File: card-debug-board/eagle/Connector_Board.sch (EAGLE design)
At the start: 32 parts, among them J1 ORESAT-DEBUG-CONNECTOR-CARD, J3 USB_A_SMT_FEMALE, Q1 MOSFET-PCH-SOT23-6, U1 FT230XS-R

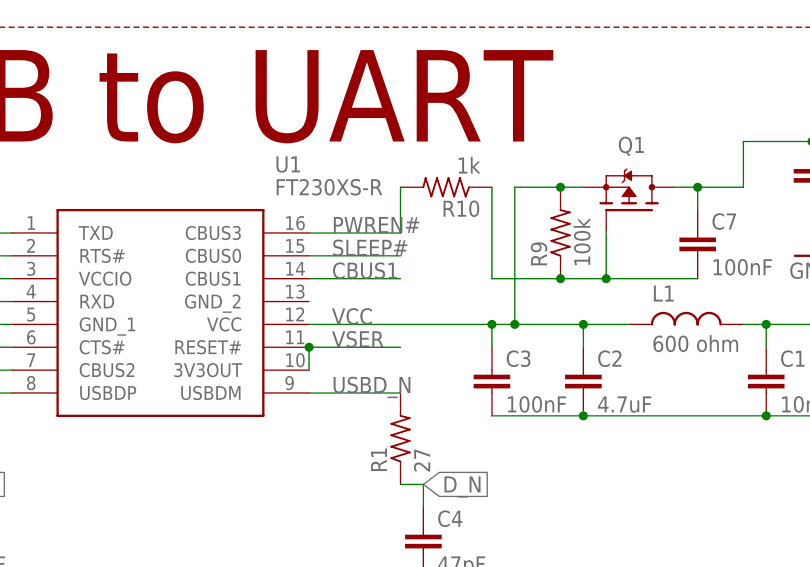
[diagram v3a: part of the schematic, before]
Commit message: clear all ERC errors
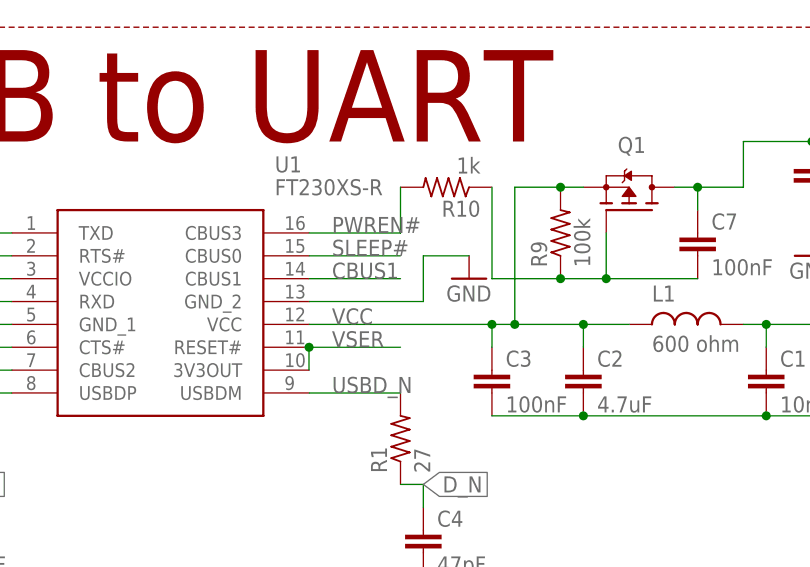
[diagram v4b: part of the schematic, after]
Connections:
- net GND: now also U1.GND_2
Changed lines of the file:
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@@
 <part name="GND12" library="supply1" library_urn="urn:adsk.eagle:library:371" deviceset="GND" device=""/>
 <part name="JP3" library="pinhead" library_urn="urn:adsk.eagle:library:325" deviceset="PINHD-1X2" device="" package3d_urn="urn:adsk.eagle:package:22435/2"/>
+<part name="GND13" library="supply1" library_urn="urn:adsk.eagle:library:371" deviceset="GND" device=""/>
 </parts>
 <sheets>
@@
 <attribute name="VALUE" x="217.17" y="48.26" size="1.778" layer="96"/>
 </instance>
+<instance part="GND13" gate="1" x="93.98" y="154.94" smashed="yes">
+<attribute name="VALUE" x="91.44" y="152.4" size="1.778" layer="96"/>
+</instance>
 </instances>
 <busses>
@@
 <wire x1="132.08" y1="162.56" x2="132.08" y2="160.02" width="0.1524" layer="91"/>
 </segment>
-</net>
+<segment>
+<pinref part="U1" gate="G$1" pin="GND_2"/>
+<wire x1="76.2" y1="152.4" x2="88.9" y2="152.4" width="0.1524" layer="91"/>
+<pinref part="GND13" gate="1" pin="GND"/>
+<wire x1="88.9" y1="152.4" x2="88.9" y2="157.48" width="0.1524" layer="91"/>
+<wire x1="88.9" y1="157.48" x2="93.98" y2="157.48" width="0.1524" layer="91"/>
+</segment>
+</net>

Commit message: Design review changes made
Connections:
- net N$1 renamed VBUS_UART
- net SLAVE_D_N renamed USB-DEVICE_D_N
- net SLAVE_D_P renamed USB-DEVICE_D_P
- new net VCCIO: C6.1, R3.2, R4.2, R5.2, R6.2, R7.2, R8.2, U1.3V3OUT, U1.RESET#, U1.VCCIO
- net VSER: now also C7.1, C8.1, Q1.D; no longer C6.1, R3.2, R4.2, R5.2, R6.2, R7.2, R8.2, U1.3V3OUT, U1.RESET#, U1.VCCIO
- net VUSB: no longer C7.1, C8.1, Q1.D
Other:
- note added: "USB DEVICE"
- note removed: "USB SLAVE"
- moved on the sheet: C1, C2, C3, C4, C5, C6, C7, C8, CM1, D2, D3, J2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

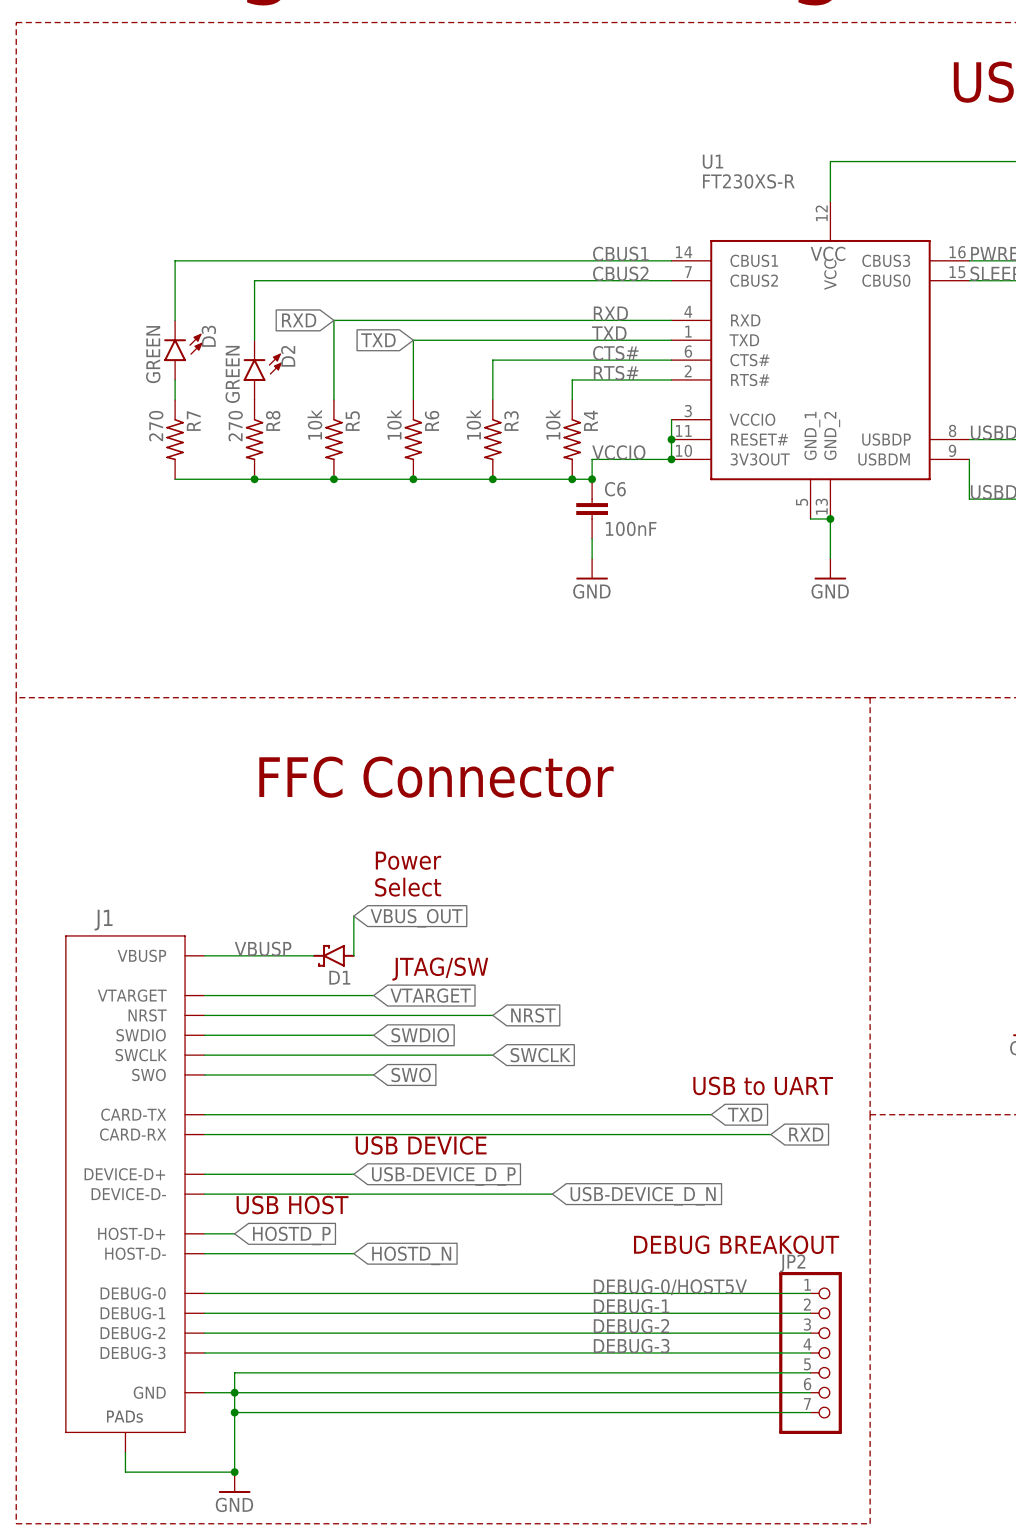
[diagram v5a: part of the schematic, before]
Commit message: Made changes per design review
Added test points for RX TX rewire, made board smaller
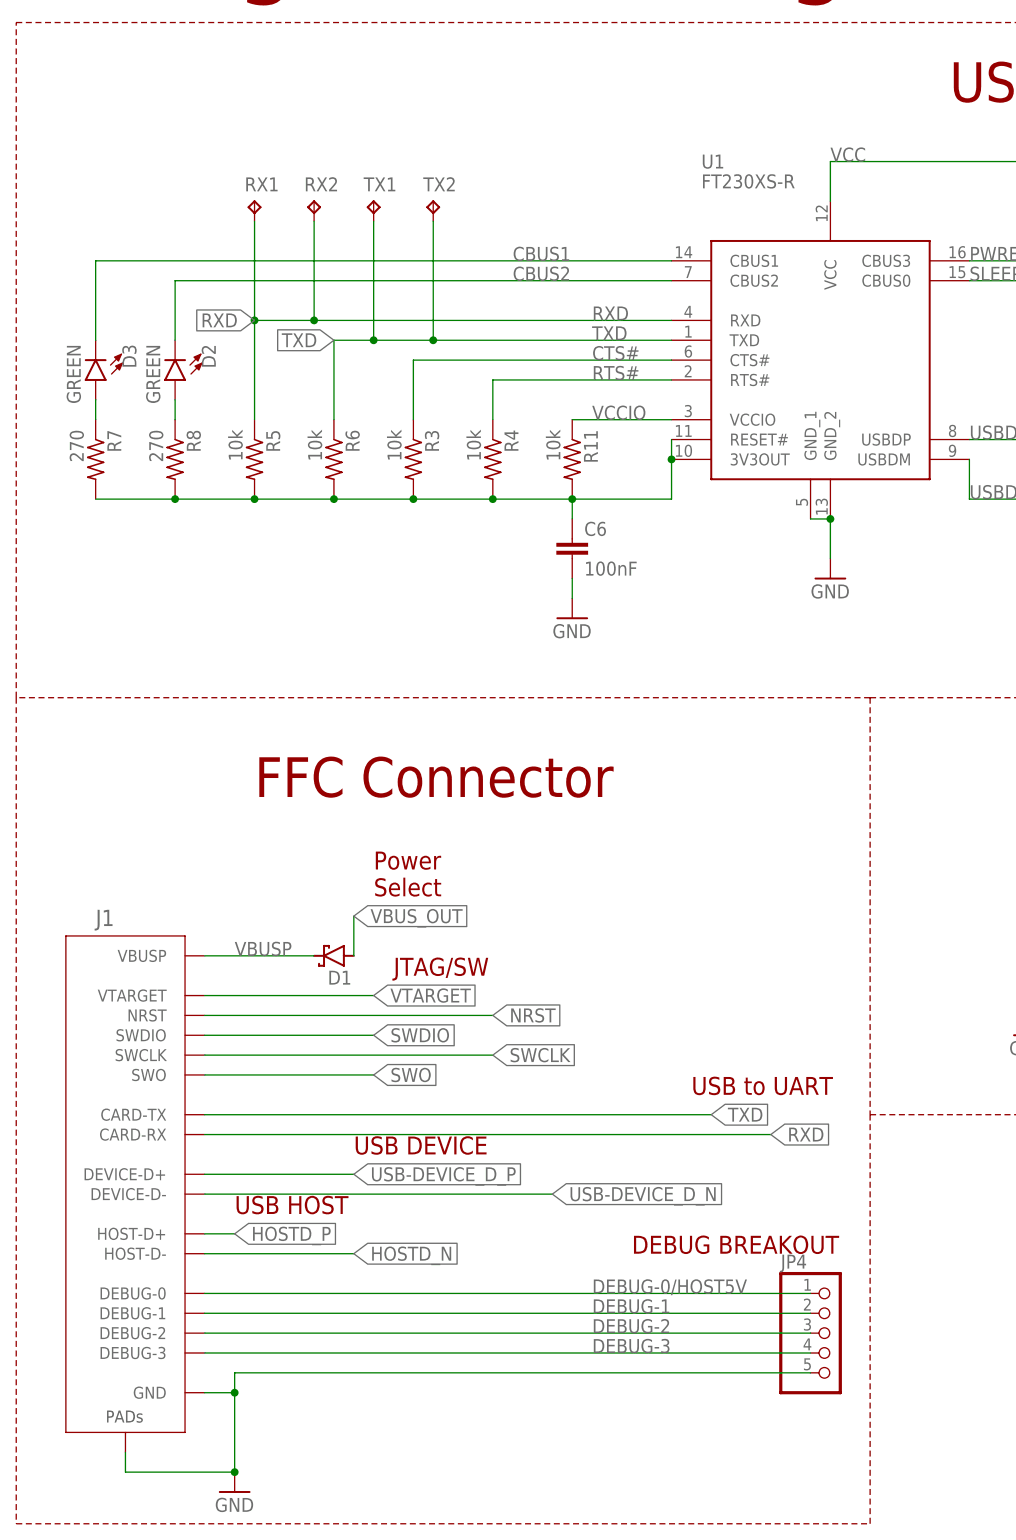
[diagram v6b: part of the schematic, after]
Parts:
- removed JP2: (no value), pinhead:PINHD-1X7
- added JP4: (no value), pinhead:PINHD-1X5
- added R11: 10k, oresat-rcl:R-US_0603-C-NOSILK
- added RX1, RX2, TX1, TX2: TP1MM-TP, oresat-misc:TP1MM-TP
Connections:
- new net VCCIO_P: C6.1, R11.2, R3.2, R4.2, R5.2, R6.2, R7.2, R8.2, U1.3V3OUT, U1.RESET#
- net DEBUG-0/HOST5V: now also JP4.1; no longer JP2.1
- net DEBUG-1: now also JP4.2; no longer JP2.2
- net DEBUG-2: now also JP4.3; no longer JP2.3
- net DEBUG-3: now also JP4.4; no longer JP2.4
- net GND: now also JP4.5; no longer JP2.5, JP2.6, JP2.7
- net RXD: now also RX1.TP, RX2.TP
- net TXD: now also TX1.TP, TX2.TP
- net VCCIO: now also R11.1; no longer C6.1, R3.2, R4.2, R5.2, R6.2, R7.2, R8.2, U1.3V3OUT, U1.RESET#
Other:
- moved on the sheet: C6, D2, D3, R3, R4, R5, R6, R7, R8

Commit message: Added masking for TX and RX
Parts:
- RX1, RX2, TX1, TX2: value TP1MM-TP -> (none)
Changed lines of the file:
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@@
 <instance part="RX1" gate="G$1" x="38.1" y="170.18" smashed="yes">
 <attribute name="NAME" x="36.83" y="171.45" size="1.778" layer="95"/>
-<attribute name="TP_SIGNAL_NAME" x="39.37" y="168.91" size="1.778" layer="97"/>
 </instance>
 <instance part="RX2" gate="G$1" x="45.72" y="170.18" smashed="yes">
 <attribute name="NAME" x="44.45" y="171.45" size="1.778" layer="95"/>
-<attribute name="TP_SIGNAL_NAME" x="46.99" y="168.91" size="1.778" layer="97"/>
 </instance>
 <instance part="TX1" gate="G$1" x="53.34" y="170.18" smashed="yes">
 <attribute name="NAME" x="52.07" y="171.45" size="1.778" layer="95"/>
-<attribute name="TP_SIGNAL_NAME" x="54.61" y="168.91" size="1.778" layer="97"/>
 </instance>
 <instance part="TX2" gate="G$1" x="60.96" y="170.18" smashed="yes">
 <attribute name="NAME" x="59.69" y="171.45" size="1.778" layer="95"/>
-<attribute name="TP_SIGNAL_NAME" x="62.23" y="168.91" size="1.778" layer="97"/>
 </instance>
 </instances>

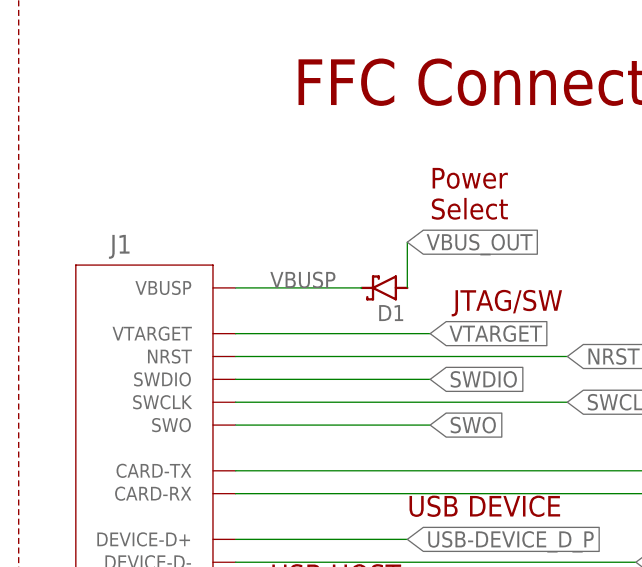
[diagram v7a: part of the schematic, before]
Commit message: Changed from VBUSP to VBUS for power out
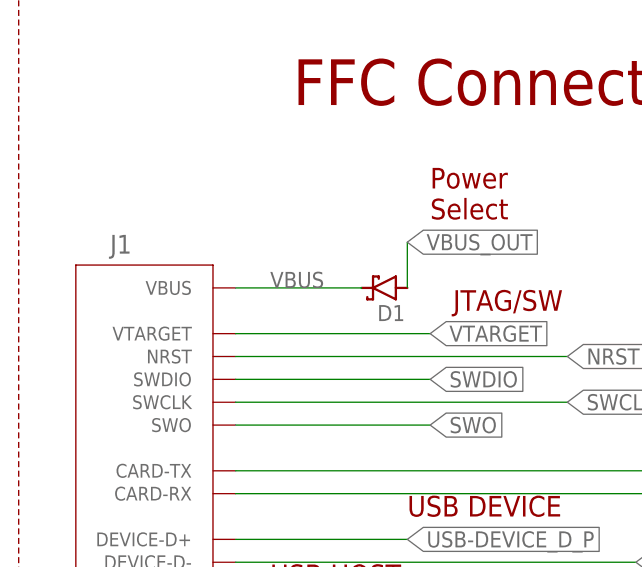
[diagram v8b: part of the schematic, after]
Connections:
- removed net VBUSP: D1.C, J1.VBUSP
- new net VBUS: D1.C, J1.VBUS
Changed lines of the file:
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@@
 </segment>
 </net>
-<net name="VBUSP" class="0">
+<net name="VBUS" class="0">
 <segment>
 <pinref part="D1" gate="G$1" pin="C"/>
 <label x="35.56" y="73.66" size="1.778" layer="95"/>
 <wire x1="45.72" y1="73.66" x2="31.75" y2="73.66" width="0.1524" layer="91"/>
-<pinref part="J1" gate="G$1" pin="VBUSP"/>
+<pinref part="J1" gate="G$1" pin="VBUS"/>
 </segment>
 </net>
